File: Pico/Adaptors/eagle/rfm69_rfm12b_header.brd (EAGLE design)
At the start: 52.4 x 18.4 mm, 5 parts

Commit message: a full panel
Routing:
- net MOSI: track 49.2 -> 48.5 mm

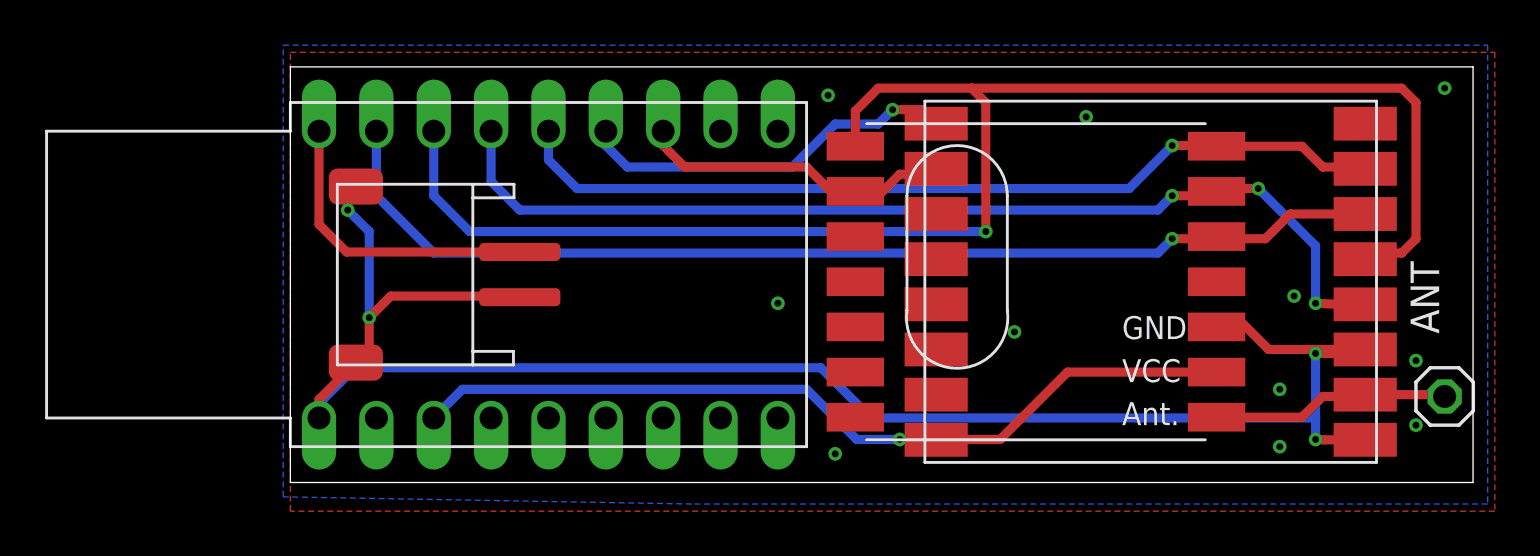
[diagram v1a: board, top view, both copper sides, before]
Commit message: Added battery charger pads to proto headers
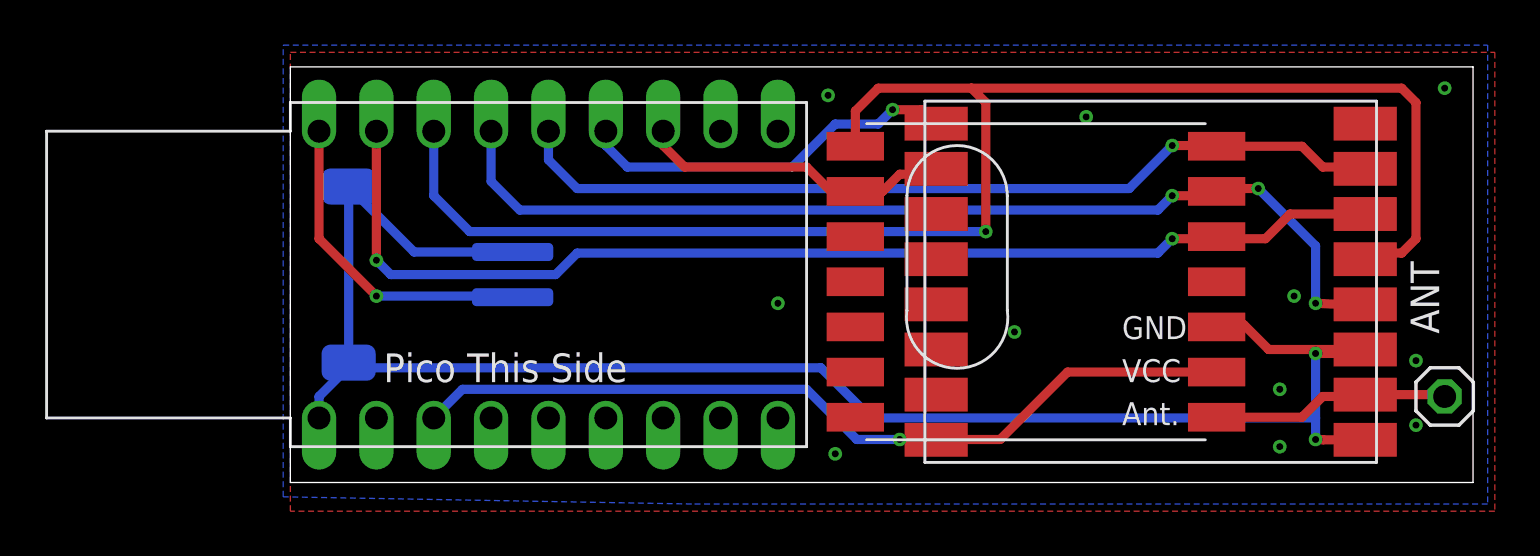
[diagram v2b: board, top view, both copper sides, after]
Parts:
- moved J1 0.32 mm to (4.76, 9.21), flipped to the bottom, turned to 90 degrees
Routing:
- net MOSI: track 48.5 -> 51.0 mm, vias 1 -> 2
- net GND: track 80.5 -> 78.4 mm, vias 15 -> 13
- net N$2: track 13.5 -> 14.4 mm, vias 0 -> 1
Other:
- board text added: "Espruino Pico RFM69HW / RFM12B rev 1.1"
- board text added: "Pico This Side"
- board text removed: "Espruino Pico RFM69HW / RFM12B rev 1.0"
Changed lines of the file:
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@@
 <layers>
 <layer number="1" name="Top" color="4" fill="1" visible="yes" active="yes"/>
-<layer number="2" name="Route2" color="1" fill="3" visible="no" active="yes"/>
-<layer number="15" name="Route15" color="4" fill="6" visible="no" active="yes"/>
 <layer number="16" name="Bottom" color="1" fill="1" visible="yes" active="yes"/>
 <layer number="17" name="Pads" color="2" fill="1" visible="yes" active="yes"/>
@@
 <wire x1="52.375" y1="18.405" x2="0" y2="18.405" width="0" layer="20"/>
 <wire x1="0" y1="18.405" x2="0" y2="0" width="0" layer="20"/>
-<text x="26.67" y="6.35" size="1.778" layer="26" rot="MR0">Espruino Pico
+<text x="40.64" y="6.35" size="1.778" layer="26" rot="MR0">Espruino Pico
 RFM69HW / RFM12B
-rev 1.0</text>
+rev 1.1</text>
+<text x="4.1275" y="4.445" size="1.27" layer="25">Pico This Side</text>
 </plain>
 <attributes>
@@
 <element name="U$3" library="RFM69" package="RFM69" value="RFM69" x="38.1" y="8.89"/>
 <element name="U$2" library="JeeParts" package="RFM12B" value="RFM12B" x="33.02" y="8.89" smashed="yes"/>
-<element name="J1" library="OPL Eagle Library" package="2P-SMD-2.0-90D" value="" x="5.08" y="9.2075" smashed="yes" rot="R270">
-<attribute name="VALUE" x="5.08" y="11.1125" size="0.635" layer="27" ratio="10" rot="R270"/>
+<element name="J1" library="OPL Eagle Library" package="2P-SMD-2.0-90D" value="" x="4.7625" y="9.2075" smashed="yes" rot="MR90">
+<attribute name="VALUE" x="4.7625" y="7.3025" size="0.635" layer="28" ratio="10" rot="MR90"/>
 </element>
 </elements>
@@
 <wire x1="45.735" y1="1.89" x2="45.4025" y2="1.905" width="0.4064" layer="1"/>
 <via x="45.4025" y="1.905" extent="1-16" drill="0.3048"/>
-<wire x1="45.4025" y1="1.905" x2="45.4025" y2="2.54" width="0.4064" layer="16"/>
+<wire x1="45.4025" y1="1.905" x2="45.4025" y2="2.8575" width="0.4064" layer="16"/>
 <via x="45.4025" y="5.715" extent="1-16" drill="0.3048"/>
 <wire x1="45.4025" y1="2.8575" x2="45.4025" y2="5.715" width="0.4064" layer="16"/>
@@
 <wire x1="42.2275" y1="6.985" x2="41.115" y2="6.985" width="0.4064" layer="1"/>
 <wire x1="41.115" y1="6.985" x2="41.02" y2="6.89" width="0.4064" layer="1"/>
-<wire x1="1.27" y1="2.8575" x2="1.27" y2="3.4925" width="0.4064" layer="16"/>
-<wire x1="1.27" y1="3.4925" x2="2.8575" y2="5.08" width="0.4064" layer="16"/>
-<wire x1="2.8575" y1="5.08" x2="23.495" y2="5.08" width="0.4064" layer="16"/>
 <wire x1="23.495" y1="5.08" x2="25.7175" y2="2.8575" width="0.4064" layer="16"/>
 <wire x1="25.7175" y1="2.8575" x2="45.4025" y2="2.8575" width="0.4064" layer="16"/>
-<wire x1="45.4025" y1="2.8575" x2="45.4025" y2="2.54" width="0.4064" layer="16"/>
 <via x="44.45" y="8.255" extent="1-16" drill="0.3048"/>
 <via x="49.8475" y="5.3975" extent="1-16" drill="0.3048"/>
@@
 <via x="24.13" y="1.27" extent="1-16" drill="0.3048"/>
 <via x="21.59" y="7.9375" extent="1-16" drill="0.3048"/>
-<via x="3.4925" y="7.3025" extent="1-16" drill="0.3048"/>
 <via x="23.8125" y="17.145" extent="1-16" drill="0.3048"/>
 <via x="35.2425" y="16.1925" extent="1-16" drill="0.3048"/>
@@
 <contactref element="J1" pad="3"/>
 <contactref element="J1" pad="4"/>
-<wire x1="2.899" y1="13.1075" x2="2.54" y2="12.7485" width="0.4064" layer="1"/>
-<wire x1="2.54" y1="12.7485" x2="2.54" y2="12.065" width="0.4064" layer="1"/>
-<via x="2.54" y="12.065" extent="1-16" drill="0.3048"/>
-<wire x1="2.54" y1="12.065" x2="3.4925" y2="11.1125" width="0.4064" layer="16"/>
-<wire x1="3.4925" y1="11.1125" x2="3.4925" y2="7.3025" width="0.4064" layer="16"/>
-<wire x1="10.16" y1="8.2075" x2="10.1125" y2="8.255" width="0.4064" layer="1"/>
-<wire x1="10.1125" y1="8.255" x2="4.445" y2="8.255" width="0.4064" layer="1"/>
-<wire x1="4.445" y1="8.255" x2="3.4925" y2="7.3025" width="0.4064" layer="1"/>
-<wire x1="2.899" y1="5.3075" x2="3.4925" y2="5.901" width="0.4064" layer="1"/>
-<wire x1="3.4925" y1="5.901" x2="3.4925" y2="7.3025" width="0.4064" layer="1"/>
-<wire x1="2.899" y1="5.3075" x2="1.27" y2="3.6785" width="0.4064" layer="1"/>
-<wire x1="1.27" y1="3.6785" x2="1.27" y2="2.8575" width="0.4064" layer="1"/>
+<wire x1="23.495" y1="5.08" x2="2.5815" y2="5.08" width="0.4064" layer="16"/>
+<wire x1="2.5815" y1="5.08" x2="2.5815" y2="5.3075" width="0.4064" layer="16"/>
+<wire x1="2.5815" y1="5.08" x2="2.54" y2="5.08" width="0.4064" layer="16"/>
+<wire x1="2.54" y1="5.08" x2="1.27" y2="3.81" width="0.4064" layer="16"/>
+<wire x1="1.27" y1="3.81" x2="1.27" y2="2.8575" width="0.4064" layer="16"/>
+<wire x1="2.5815" y1="5.3075" x2="2.5815" y2="13.1075" width="0.4064" layer="16"/>
+<wire x1="9.8425" y1="10.2075" x2="5.4815" y2="10.2075" width="0.4064" layer="16"/>
+<wire x1="5.4815" y1="10.2075" x2="2.5815" y2="13.1075" width="0.4064" layer="16"/>
 </signal>
 <signal name="3.3V">
@@
 <via x="39.0525" y="10.795" extent="1-16" drill="0.3048"/>
 <wire x1="39.0525" y1="10.795" x2="38.4175" y2="10.16" width="0.4064" layer="16"/>
-<wire x1="38.4175" y1="10.16" x2="6.35" y2="10.16" width="0.4064" layer="16"/>
-<wire x1="6.35" y1="10.16" x2="3.81" y2="12.7" width="0.4064" layer="16"/>
-<wire x1="3.81" y1="12.7" x2="3.81" y2="15.5575" width="0.4064" layer="16"/>
+<wire x1="38.4175" y1="10.16" x2="12.7" y2="10.16" width="0.4064" layer="16"/>
+<wire x1="12.7" y1="10.16" x2="11.7475" y2="9.2075" width="0.4064" layer="16"/>
+<wire x1="11.7475" y1="9.2075" x2="4.445" y2="9.2075" width="0.4064" layer="16"/>
+<wire x1="4.445" y1="9.2075" x2="3.81" y2="9.8425" width="0.4064" layer="16"/>
+<via x="3.81" y="9.8425" extent="1-16" drill="0.3048"/>
+<wire x1="3.81" y1="9.8425" x2="3.81" y2="15.5575" width="0.4064" layer="1"/>
 </signal>
 <signal name="MISO">
@@
 <contactref element="U$1" pad="BAT"/>
 <contactref element="J1" pad="+"/>
-<wire x1="1.27" y1="15.5575" x2="1.27" y2="11.43" width="0.4064" layer="1"/>
-<wire x1="1.27" y1="11.43" x2="2.4925" y2="10.2075" width="0.4064" layer="1"/>
-<wire x1="2.4925" y1="10.2075" x2="10.16" y2="10.2075" width="0.4064" layer="1"/>
+<wire x1="1.27" y1="15.5575" x2="1.27" y2="10.795" width="0.4064" layer="1"/>
+<wire x1="1.27" y1="10.795" x2="3.81" y2="8.255" width="0.4064" layer="1"/>
+<via x="3.81" y="8.255" extent="1-16" drill="0.3048"/>
+<wire x1="3.81" y1="8.255" x2="9.795" y2="8.255" width="0.4064" layer="16"/>
+<wire x1="9.795" y1="8.255" x2="9.8425" y2="8.2075" width="0.4064" layer="16"/>
 </signal>
 </signals>
